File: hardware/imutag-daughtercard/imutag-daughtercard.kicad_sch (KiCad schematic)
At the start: 34 parts, among them J1 Conn_01x05, J2 Conn_01x06, J3 CONN_01X02, J4 Conn_01x04, J6 Conn_01x04, J7 Conn_01x04, J8 Conn_01x05, Q1 Q_NPN_BEC, U2 LPS22DF, U3 stm32l431kc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

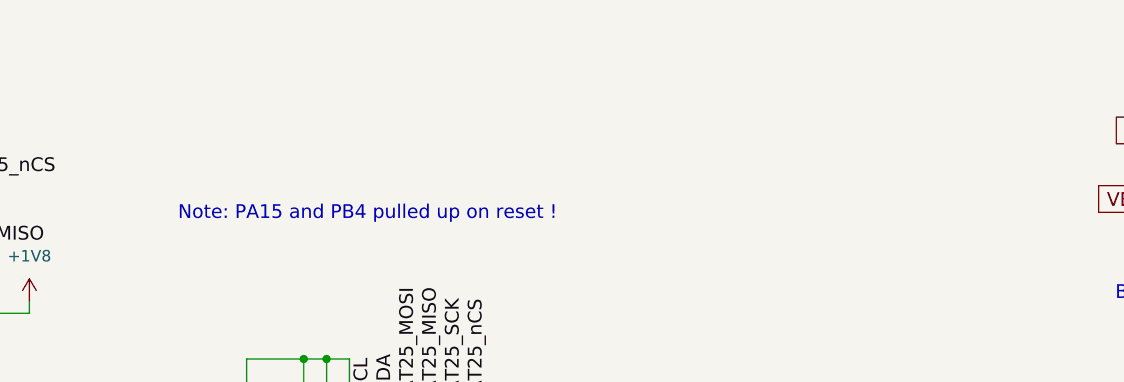
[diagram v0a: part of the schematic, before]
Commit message: imu tag breakout
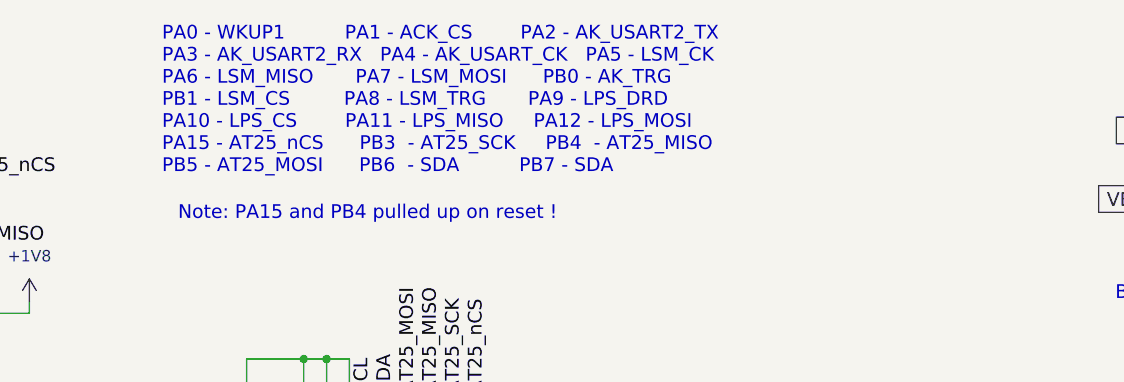
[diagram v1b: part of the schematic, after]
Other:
- note added: "PA0 - WKUP1 PA1 - ACK_CS PA2 - AK_USART2_TX PA3 - AK_USART2_RX PA4 - AK_USART_CK PA5 - LSM_CK PA6 - LSM_MISO PA7 - LSM_MOSI PB0 - AK_TRG PB1 - LSM_CS PA8 - LSM_TRG PA9 - LPS_DRD PA10 - LPS_CS PA11 - LPS_MISO PA12 - LPS_MOSI PA15 - AT25_nCS PB3 - AT25_SCK PB4 - AT25_MISO PB5 - AT25_MOSI PB6 - SDA PB7 - SDA"
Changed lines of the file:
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@@
 (kicad_sch
-	(version 20231120)
+	(version 20250114)
 	(generator "eeschema")
-	(generator_version "8.0")
+	(generator_version "9.0")
 	(paper "USLetter")
 	(title_block
@@
 		(rev "7 ")
 	)
+	(text "Battery"
+		(exclude_from_sim no)
+		(at 198.12 45.72 0)
+		(effects
+			(font
+				(size 1.524 1.524)
+			)
+			(justify left bottom)
+		)
+	)
+	(text "Add test points"
+		(exclude_from_sim no)
+		(at 91.44 166.37 0)
+		(effects
+			(font
+				(size 1.27 1.27)
+			)
+		)
+	)
+	(text "PA0 - WKUP1          PA1 - ACK_CS        PA2 - AK_USART2_TX\nPA3 - AK_USART2_RX   PA4 - AK_USART_CK   PA5 - LSM_CK\nPA6 - LSM_MISO       PA7 - LSM_MOSI      PB0 - AK_TRG\nPB1 - LSM_CS         PA8 - LSM_TRG       PA9 - LPS_DRD\nPA10 - LPS_CS        PA11 - LPS_MISO     PA12 - LPS_MOSI\nPA15 - AT25_nCS      PB3  - AT25_SCK     PB4  - AT25_MISO\nPB5 - AT25_MOSI      PB6  - SDA          PB7 - SDA"
+		(exclude_from_sim no)
+		(at 92.202 23.368 0)
+		(effects
+			(font
+				(face "Courier")
+				(size 1.524 1.524)
+			)
+			(justify left)
+		)
+	)
+	(text "Note: PA15 and PB4 pulled up on reset !"
+		(exclude_from_sim no)
+		(at 93.98 36.83 0)
+		(effects
+			(font
+				(size 1.524 1.524)
+			)
+			(justify left bottom)
+		)
+	)
 	(junction
 		(at 175.26 133.35)
@@
 		)
 	)
-	(text "Battery"
-		(exclude_from_sim no)
-		(at 198.12 45.72 0)
-		(effects
-			(font
-				(size 1.524 1.524)
-			)
-			(justify left bottom)
-		)
-	)
-	(text "Add test points"
-		(exclude_from_sim no)
-		(at 91.44 166.37 0)
-		(effects
-			(font
-				(size 1.27 1.27)
-			)
-		)
-	)
-	(text "Note: PA15 and PB4 pulled up on reset !"
-		(exclude_from_sim no)
-		(at 93.98 36.83 0)
-		(effects
-			(font
-				(size 1.524 1.524)
-			)
-			(justify left bottom)
-		)
-	)
 	(label "AT25_MISO"
 		(at 123.19 55.88 90)
-		(fields_autoplaced yes)
 		(effects
 			(font
@@
 	(label "AT25_SCK"
 		(at 80.01 193.04 180)
-		(fields_autoplaced yes)
 		(effects
 			(font
@@
 	(label "LSM_CK"
 		(at 114.3 191.77 180)
-		(fields_autoplaced yes)
 		(effects
 			(font
@@
 	(label "SCL"
 		(at 207.01 67.31 180)
-		(fields_autoplaced yes)
 		(effects
 			(font
@@
 	(label "LSM_MOSI"
 		(at 114.3 189.23 180)
-		(fields_autoplaced yes)
 		(effects
 			(font
@@
 	(label "AK_CS"
 		(at 114.3 171.45 180)
-		(fields_autoplaced yes)
 		(effects
 			(font
@@
 	(label "AT25_nCS"
 		(at 69.85 31.75 0)
-		(fields_autoplaced yes)
 		(effects
 			(font
@@
 	(label "USART1_CK"
 		(at 72.39 139.7 0)
-		(fields_autoplaced yes)
 		(effects
 			(font
@@
 	(label "AK_USART2_TX"
 		(at 114.3 168.91 180)
-		(fields_autoplaced yes)
 		(effects
 			(font
@@
 	(label "AK_RSTN"
 		(at 114.3 179.07 180)
-		(fields_autoplaced yes)
 		(effects
 			(font
@@
 	(label "AK_RSTN"
 		(at 236.22 93.98 0)
-		(fields_autoplaced yes)
 		(effects
 			(font
@@
 	(label "USART1_RX"
 		(at 151.13 91.44 0)
-		(fields_autoplaced yes)
 		(effects
 			(font
@@
 	(label "LSM_MISO"
 		(at 189.23 128.27 180)
-		(fields_autoplaced yes)
 		(effects
 			(font
@@
 	(label "LSM_MOSI"
 		(at 240.03 128.27 0)
-		(fields_autoplaced yes)
 		(effects
 			(font
@@
 	(label "USART1_TX"
 		(at 72.39 134.62 0)
-		(fields_autoplaced yes)
 		(effects
 			(font
@@
 	(label "AK_USART2_RX"
 		(at 246.38 106.68 270)
-		(fields_autoplaced yes)
 		(effects
 			(font
@@
 	(label "LPS_CS"
 		(at 80.01 171.45 180)
-		(fields_autoplaced yes)
 		(effects
 			(font
@@
 	(label "LPS_CS"
 		(at 72.39 142.24 0)
-		(fields_autoplaced yes)
 		(effects
 			(font
@@
 	(label "LSM_MISO"
 		(at 115.57 121.92 270)
-		(fields_autoplaced yes)
 		(effects
 			(font
@@
 	(label "AT25_SCK"
 		(at 43.18 46.99 180)
-		(fields_autoplaced yes)
 		(effects
 			(font
@@
 	(label "AK_USART2_CK"
 		(at 185.42 99.06 180)
-		(fields_autoplaced yes)
 		(effects
 			(font
@@
 	(label "WKUP1"
 		(at 85.09 91.44 180)
-		(fields_autoplaced yes)
 		(effects
 			(font
@@
 	(label "SCL"
 		(at 115.57 55.88 90)
-		(fields_autoplaced yes)
 		(effects
 			(font
@@
 	(label "LSM_MISO"
 		(at 114.3 194.31 180)
-		(fields_autoplaced yes)
 		(effects
 			(font
@@
 	(label "AK_USART2_CK"
 		(at 114.3 173.99 180)
-		(fields_autoplaced yes)
 		(effects
 			(font
@@
 	(label "SDA"
 		(at 207.01 69.85 180)
-		(fields_autoplaced yes)
 		(effects
 			(font
@@
 	(label "WKUP1"
 		(at 114.3 196.85 180)
-		(fields_autoplaced yes)
 		(effects
 			(font
@@
 	(label "LSM_MOSI"
 		(at 118.11 121.92 270)
-		(fields_autoplaced yes)
 		(effects
 			(font
@@
 	(label "AT25_MISO"
 		(at 80.01 190.5 180)
-		(fields_autoplaced yes)
 		(effects
 			(font
@@
 	(label "AK_USART2_TX"
 		(at 185.42 101.6 180)
-		(fields_autoplaced yes)
 		(effects
 			(font
@@
 	(label "AT25_MOSI"
 		(at 80.01 187.96 180)
-		(fields_autoplaced yes)
 		(effects
 			(font
@@
 	(label "AK_USART2_RX"
 		(at 114.3 176.53 180)
-		(fields_autoplaced yes)
 		(effects
 			(font
@@
 	(label "AK_RSTN"
 		(at 120.65 121.92 270)
-		(fields_autoplaced yes)
 		(effects
 			(font
@@
 	(label "LSM_CS"
 		(at 123.19 121.92 270)
-		(fields_autoplaced yes)
 		(effects
 			(font
@@
 	(label "AT25_nCS"
 		(at 80.01 195.58 180)
-		(fields_autoplaced yes)
 		(effects
 			(font
@@
 	(label "WKUP1"
 		(at 189.23 135.89 180)
-		(fields_autoplaced yes)
 		(effects
 			(font
@@
 	(label "USART1_TX"
 		(at 80.01 173.99 180)
-		(fields_autoplaced yes)
 		(effects
 			(font
@@
 	(label "LPS_CS"
 		(at 151.13 86.36 0)
-		(fields_autoplaced yes)
 		(effects
 			(font
@@
 	(label "AT25_MOSI"
 		(at 43.18 54.61 180)
-		(fields_autoplaced yes)
 		(effects
 			(font
@@
 	(label "USART1_CK"
 		(at 80.01 179.07 180)
-		(fields_autoplaced yes)
 		(effects
 			(font
@@
 	(label "AT25_nCS"
 		(at 128.27 55.88 90)
-		(fields_autoplaced yes)
 		(effects
 			(font
@@
 	(label "clkout"
 		(at 207.01 62.23 180)
-		(fields_autoplaced yes)
 		(effects
 			(font
@@
 	(label "AT25_MISO"
 		(at 67.31 39.37 0)
-		(fields_autoplaced yes)
 		(effects
 			(font
@@
 	(label "USART1_RX"
 		(at 72.39 137.16 0)
-		(fields_autoplaced yes)
 		(effects
 			(font
@@
 	(label "LSM_CK"
 		(at 113.03 121.92 270)
-		(fields_autoplaced yes)
 		(effects
 			(font
@@
 	(label "USART1_CK"
 		(at 151.13 96.52 0)
-		(fields_autoplaced yes)
 		(effects
 			(font
@@
 	(label "AK_CS"
 		(at 185.42 96.52 180)
-		(fields_autoplaced yes)
 		(effects
 			(font
@@
 	(label "AK_USART2_TX"
 		(at 81.28 96.52 180)
-		(fields_autoplaced yes)
 		(effects
 			(font
@@
 	(label "AT25_MOSI"
 		(at 120.65 55.88 90)
-		(fields_autoplaced yes)
 		(effects
 			(font
@@
 	(label "USART1_TX"
 		(at 151.13 93.98 0)
-		(fields_autoplaced yes)
 		(effects
 			(font
@@
 	(label "LSM_CS"
 		(at 240.03 133.35 0)
-		(fields_autoplaced yes)
 		(effects
 			(font
@@
 	(label "clkout"
 		(at 77.47 81.28 180)
-		(fields_autoplaced yes)
 		(effects
 			(font
@@
 	(label "AT25_SCK"
 		(at 125.73 55.88 90)
-		(fields_autoplaced yes)
 		(effects
 			(font
@@
 	(label "AK_CS"
 		(at 85.09 93.98 180)
-		(fields_autoplaced yes)
 		(effects
 			(font
@@
 	(label "AK_USART2_CK"
 		(at 110.49 121.92 270)
-		(fields_autoplaced yes)
 		(effects
 			(font
@@
 	(label "AK_USART2_RX"
 		(at 107.95 121.92 270)
-		(fields_autoplaced yes)
 		(effects
 			(font
@@
 	(label "SDA"
 		(at 118.11 55.88 90)
-		(fields_autoplaced yes)
 		(effects
 			(font
@@
 	(label "LSM_CS"
 		(at 114.3 186.69 180)
-		(fields_autoplaced yes)
 		(effects
 			(font
@@
 	(label "LSM_CK"
 		(at 240.03 130.81 0)
-		(fields_autoplaced yes)
 		(effects
 			(font
@@
 	(label "USART1_RX"
 		(at 80.01 176.53 180)
-		(fields_autoplaced yes)
 		(effects
 			(font
@@
 		)
 	)
+	(embedded_fonts no)
 )
